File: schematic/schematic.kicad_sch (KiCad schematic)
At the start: 34 parts

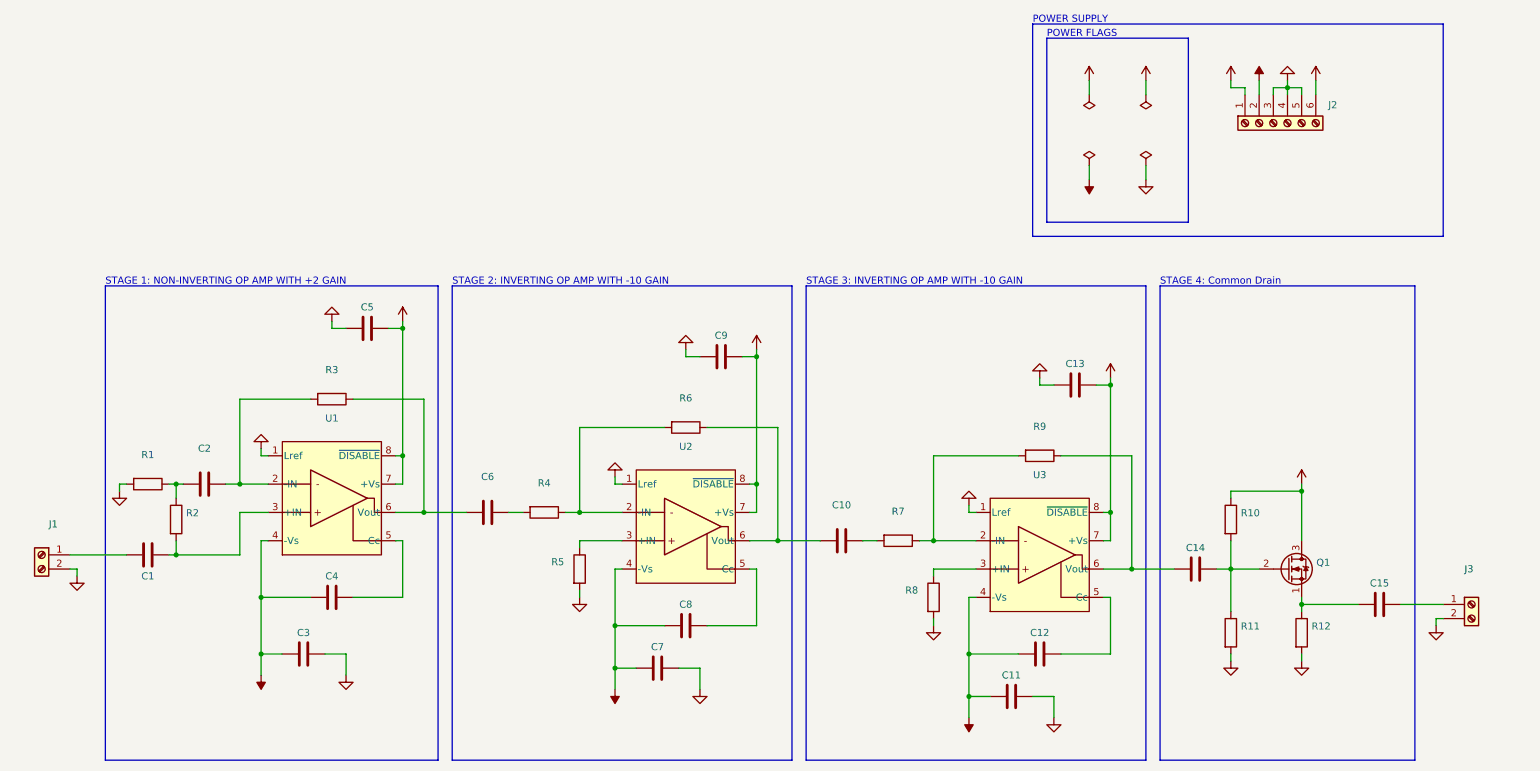
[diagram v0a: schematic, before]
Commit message: [PCB] Flip power connector
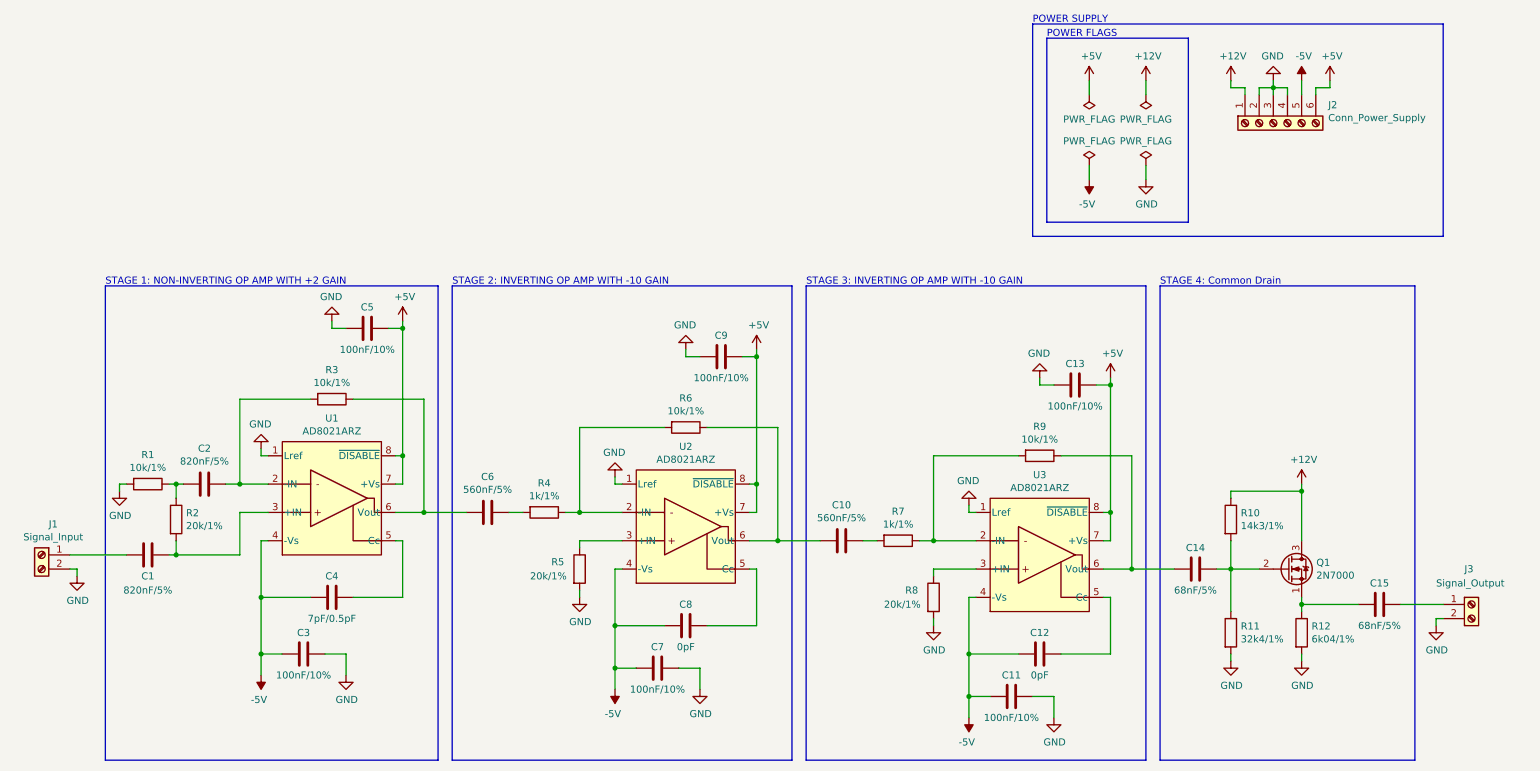
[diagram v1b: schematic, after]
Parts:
- C1, C2: value (none) -> 820nF/5%; footprint (none) -> Capacitor_SMD:C_0603_1608Metric_Pad1.08x0.95mm_HandSolder
- C10, C6: value (none) -> 560nF/5%; footprint (none) -> Capacitor_SMD:C_0603_1608Metric_Pad1.08x0.95mm_HandSolder
- C11, C13, C3, C5, C7, C9: value (none) -> 100nF/10%; footprint (none) -> Capacitor_SMD:C_0603_1608Metric_Pad1.08x0.95mm_HandSolder
- C12, C8: value (none) -> 0pF; footprint (none) -> Capacitor_SMD:C_0603_1608Metric_Pad1.08x0.95mm_HandSolder
- C14, C15: value (none) -> 68nF/5%; footprint (none) -> Capacitor_SMD:C_0603_1608Metric_Pad1.08x0.95mm_HandSolder
- C4: value (none) -> 7pF/0.5pF; footprint (none) -> Capacitor_SMD:C_0603_1608Metric_Pad1.08x0.95mm_HandSolder
- J1: value (none) -> Signal_Input; footprint (none) -> TerminalBlock:TerminalBlock_bornier-2_P5.08mm
- J2: value (none) -> Conn_Power_Supply; footprint (none) -> TerminalBlock:TerminalBlock_bornier-6_P5.08mm
- J3: value (none) -> Signal_Output; footprint (none) -> TerminalBlock:TerminalBlock_bornier-2_P5.08mm
- Q1: value (none) -> 2N7000; footprint (none) -> Package_TO_SOT_THT:TO-92_Inline
- R1, R3, R6, R9: value (none) -> 10k/1%; footprint (none) -> Resistor_SMD:R_0603_1608Metric_Pad0.98x0.95mm_HandSolder
- R10: value (none) -> 14k3/1%; footprint (none) -> Resistor_SMD:R_0603_1608Metric_Pad0.98x0.95mm_HandSolder
- R11: value (none) -> 32k4/1%; footprint (none) -> Resistor_SMD:R_0603_1608Metric_Pad0.98x0.95mm_HandSolder
- R12: value (none) -> 6k04/1%; footprint (none) -> Resistor_SMD:R_0603_1608Metric_Pad0.98x0.95mm_HandSolder
- R2, R5, R8: value (none) -> 20k/1%; footprint (none) -> Resistor_SMD:R_0603_1608Metric_Pad0.98x0.95mm_HandSolder
- R4, R7: value (none) -> 1k/1%; footprint (none) -> Resistor_SMD:R_0603_1608Metric_Pad0.98x0.95mm_HandSolder
- U1, U2, U3: value (none) -> AD8021ARZ; footprint (none) -> Package_SO:SOIC-8_3.9x4.9mm_P1.27mm
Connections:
- net +12V: now also J2.1 (Pin_1); no longer J2.6 (Pin_6)
- net +5V: now also J2.6 (Pin_6); no longer J2.1 (Pin_1)
- net -5V: now also J2.5 (Pin_5); no longer J2.2 (Pin_2)
- net GND: now also J2.2 (Pin_2); no longer J2.5 (Pin_5)

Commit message: [Docs] Add project documentation
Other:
- note added: "STAGE 4: COMMON DRAIN"
- note removed: "STAGE 4: Common Drain"
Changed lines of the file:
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@@
     (effects (font (size 1.27 1.27)) (justify left bottom))
   )
-  (text "STAGE 4: Common Drain" (at 220.98 73.66 0)
+  (text "STAGE 4: COMMON DRAIN" (at 220.98 73.66 0)
     (effects (font (size 1.27 1.27)) (justify left bottom))
   )
